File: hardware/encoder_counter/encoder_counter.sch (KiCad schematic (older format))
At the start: 29 parts, among them P1 MOLEX_HEADER, P10 FEMALE_HEADER, P11 TERM_BLOCK_CON, P2 MOLEX_HEADER, P3 FEMALE_HEADER, P4 FEMALE_HEADER, P5 MOLEX_HEADER, P6 MOLEX_HEADER, P7 FEMALE_HEADER, P8 FEMALE_HEADER, P9 CONN_01X03, U1 LM7812, U5 LS7366R, U6 LS7366R, Y1 20 MHz, Y2 20 MHz

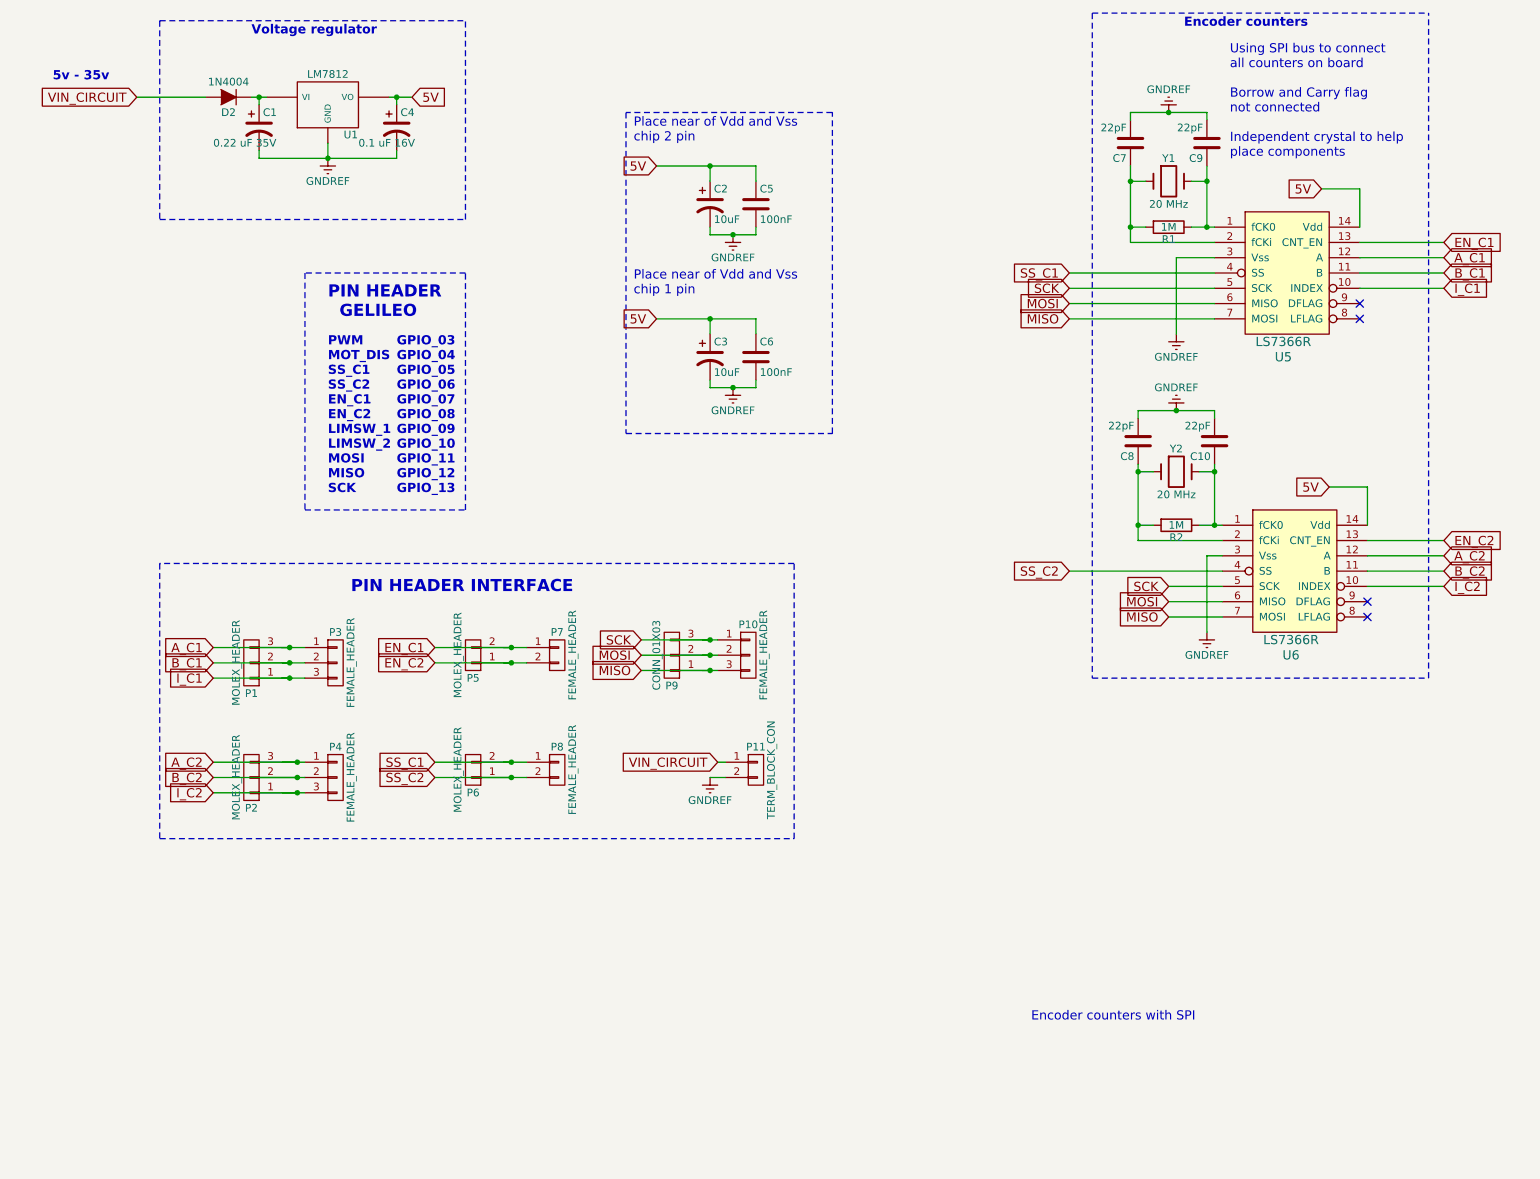
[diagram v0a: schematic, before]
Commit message: Added PID, LS7366R lib and layout off DC Motor Driver PCB and Arduino Shied PCB.
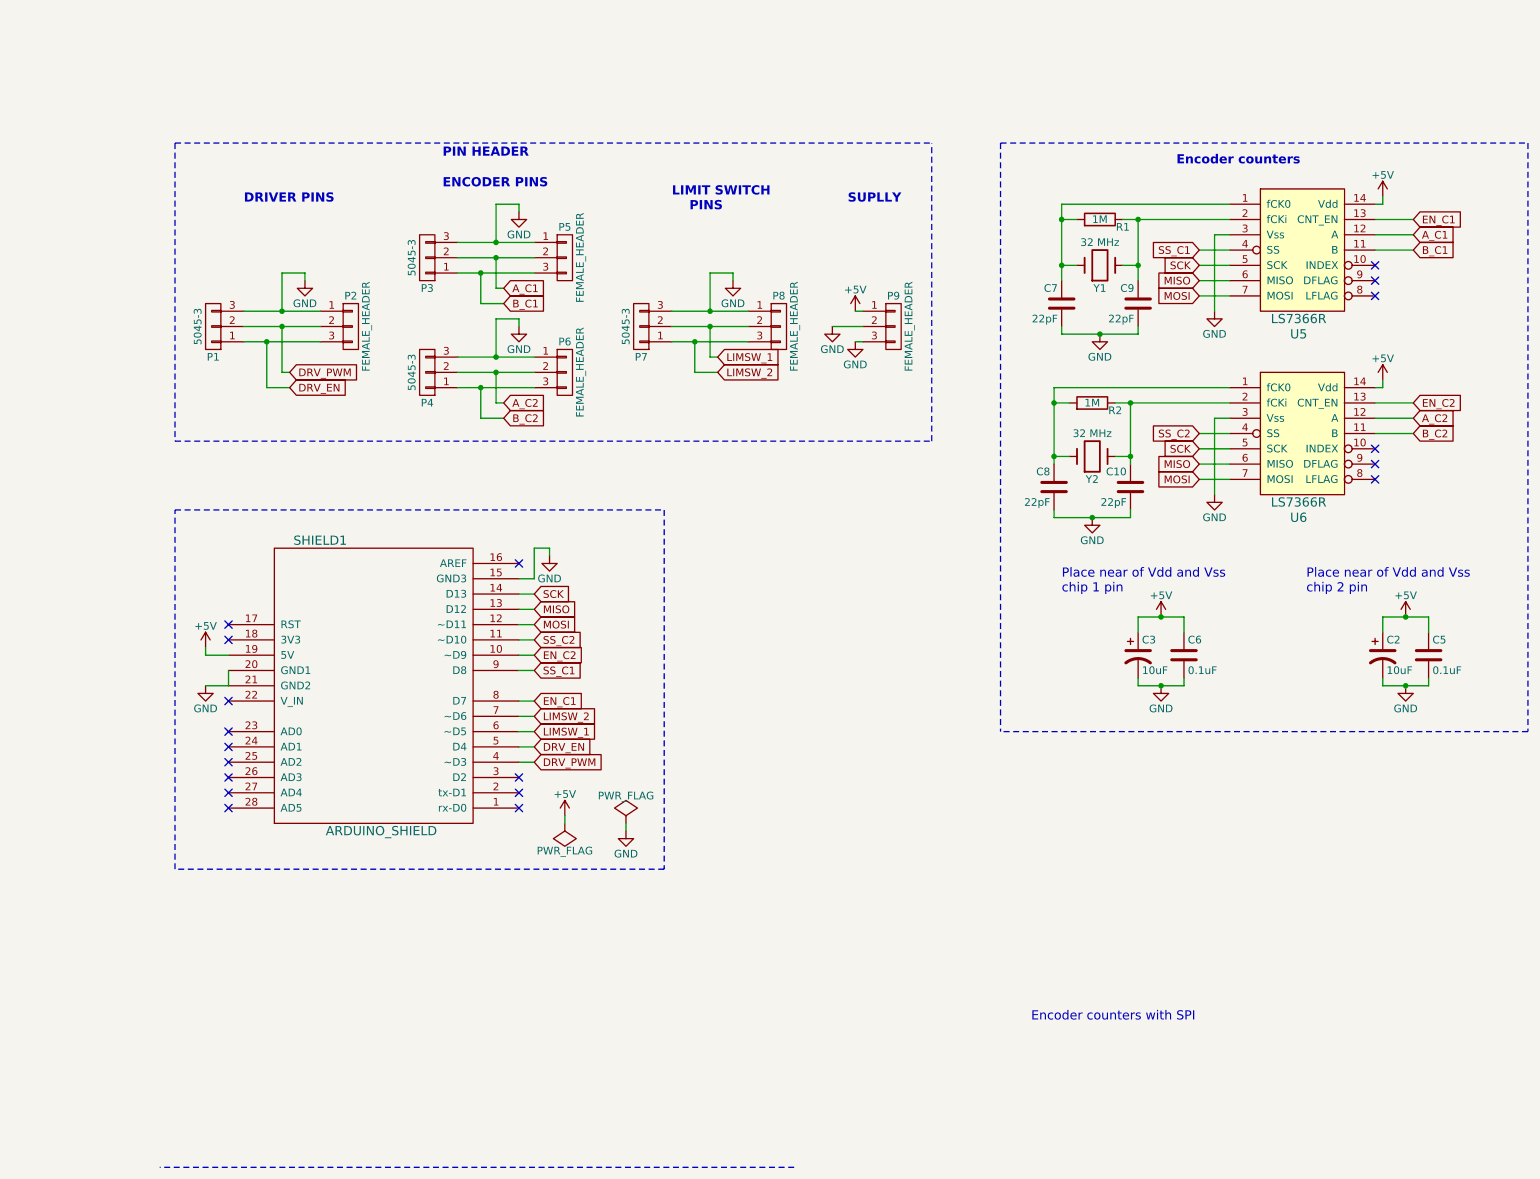
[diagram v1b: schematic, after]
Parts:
- removed C1: 0.22 uF 35V, symbol CP1
- removed C4: 0.1 uF 16V, symbol CP1
- removed D2: 1N4004, symbol D
- removed P10: FEMALE_HEADER, symbol CONN_01X03
- removed P11: TERM_BLOCK_CON, symbol CONN_01X02
- removed P5, P6: MOLEX_HEADER, symbol CONN_01X02
- removed P7, P8: FEMALE_HEADER, symbol CONN_01X02
- removed U1: LM7812, symbol LM7812
- added P5, P6, P8: FEMALE_HEADER, Maplex_Misc:Pin_Header_Straight_1x03_Pitch2.54mm, symbol CONN_01X03
- added P7: 5045-3, Maplex_Misc:Molex_3Pin_180_TH, symbol CONN_01X03
- added SHIELD1: ARDUINO_SHIELD, Maplex_Misc:ARDUINO_SHIELD, symbol ARDUINO_SHIELD
- C10, C7, C8, C9: footprint (none) -> Maplex_Misc:C_Disc_D3.4mm_W2.1mm_P2.50mm
- C2, C3: footprint (none) -> Maplex_Misc:CP_Radial_D6.3mm_P2.50mm
- C5, C6: value 100nF -> 0.1uF; footprint (none) -> Maplex_Misc:C_Disc_D5.0mm_W2.5mm_P2.50mm
- P1: value MOLEX_HEADER -> 5045-3; footprint (none) -> Maplex_Misc:Molex_3Pin_180_TH
- P2: value MOLEX_HEADER -> FEMALE_HEADER; footprint (none) -> Maplex_Misc:Pin_Header_Straight_1x03_Pitch2.54mm
- P3, P4: value FEMALE_HEADER -> 5045-3; footprint (none) -> Maplex_Misc:Molex_3Pin_180_TH
- P9: value CONN_01X03 -> FEMALE_HEADER; footprint (none) -> Maplex_Misc:Pin_Header_Straight_1x03_Pitch2.54mm
- R1, R2: footprint (none) -> Maplex_Misc:Resistor_Horizontal_RM10mm_L7mm
- U5, U6: footprint (none) -> Maplex_Misc:DIP-14_W15.24mm_Socket_Header
- Y1, Y2: value 20 MHz -> 32 MHz; footprint (none) -> Maplex_Misc:Crystal_HC18-U_Vertical
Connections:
- net A_C1: now also P3.2 (P2), P5.2 (P2); no longer P1.3 (P3), P3.1 (P1)
- net A_C2: now also P4.2 (P2), P6.2 (P2); no longer P2.3 (P3), P4.1 (P1)
- net B_C1: now also P3.1 (P1), P5.3 (P3); no longer P1.2 (P2), P3.2 (P2)
- net B_C2: now also P4.1 (P1), P6.3 (P3); no longer P2.2 (P2), P4.2 (P2)
- net EN_C1: now also SHIELD1.8 (D7)
- net EN_C2: now also SHIELD1.10 (~~D9)
- net MISO: now also U5.6 (MISO), U6.6 (MISO), SHIELD1.13 (D12); no longer P9.1 (P1), U5.7 (MOSI), U6.7 (MOSI)
- net MOSI: now also U5.7 (MOSI), U6.7 (MOSI), SHIELD1.12 (~~D11); no longer P9.2 (P2), U5.6 (MISO), U6.6 (MISO)
- net SCK: now also SHIELD1.14 (D13); no longer P9.3 (P3)
- net SS_C1: now also SHIELD1.9 (D8)
- net SS_C2: now also SHIELD1.11 (~~D10)
- net at C9.1, R1.1, Y1.2: now also U5.2 (fCKi); no longer U5.1 (fCK0)
- net at C7.1, R1.2, Y1.1: now also U5.1 (fCK0); no longer U5.2 (fCKi)
- net at C10.1, R2.1, Y2.2: now also U6.2 (fCKi); no longer U6.1 (fCK0)
- net at C8.1, R2.2, Y2.1: now also U6.1 (fCK0); no longer U6.2 (fCKi)
- net 5V renamed +5V
- net +5V: now also P9.1 (P1), SHIELD1.19 (5V)
- net GNDREF renamed GND
- net GND: now also P1.3 (P3), P2.1 (P1), P3.3 (P3), P4.3 (P3), P9.2 (P2), P9.3 (P3), P5.1 (P1), P6.1 (P1), P7.3 (P3), P8.1 (P1), SHIELD1.15 (GND3), SHIELD1.20 (GND1), SHIELD1.21 (GND2)
- removed net I_C1: P1.1 (P1), P3.3 (P3), U5.10 (INDEX)
- removed net I_C2: P2.1 (P1), P4.3 (P3), U6.10 (INDEX)
- new net DRV_EN: P1.1 (P1), P2.3 (P3), SHIELD1.5 (D4)
- new net DRV_PWM: P1.2 (P2), P2.2 (P2), SHIELD1.4 (~~D3)
- new net LIMSW_1: P7.2 (P2), P8.2 (P2), SHIELD1.6 (~~D5)
- new net LIMSW_2: P7.1 (P1), P8.3 (P3), SHIELD1.7 (~~D6)
- no-connect marks 4 -> 19
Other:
- note added: "DRIVER PINS"
- note added: "ENCODER PINS"
- note added: "LIMIT SWITCH\n PINS"
- note added: "PIN HEADER"
- note added: "SUPLLY"
- note removed: "5v - 35v"
- note removed: "GPIO_03\nGPIO_04\nGPIO_05\nGPIO_06\nGPIO_07\nGPIO_08\nGPIO_09\nGPIO_10\nGPIO_11\nGPIO_12\nGPIO_13"
- note removed: "PIN HEADER INTERFACE"
- note removed: "PIN HEADER\n GELILEO"
- note removed: "PWM\nMOT_DIS\nSS_C1\nSS_C2\nEN_C1\nEN_C2\nLIMSW_1\nLIMSW_2\nMOSI\nMISO\nSCK"
- note removed: "Using SPI bus to connect\nall counters on board\n\nBorrow and Carry flag\nnot connected\n\nIndependent crystal to help \nplace components"
- note removed: "Voltage regulator"
- moved on the sheet: C10, C2, C3, C5, C6, C7, C8, C9, R1, R2, U5, U6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

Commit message: Last version.
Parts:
- removed P1, P3, P4, P7: 5045-3, Maplex_Misc:Molex_3Pin_180_TH, symbol CONN_01X03
- removed P2, P5, P6, P8, P9: FEMALE_HEADER, Maplex_Misc:Pin_Header_Straight_1x03_Pitch2.54mm, symbol CONN_01X03
- SHIELD1: value ARDUINO_SHIELD -> GALILEO_SHIELD
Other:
- note removed: "DRIVER PINS"
- note removed: "ENCODER PINS"
- note removed: "LIMIT SWITCH\n PINS"
- note removed: "PIN HEADER"
- note removed: "SUPLLY"
- moved on the sheet: C10, C2, C3, C5, C6, C7, C8, C9, R1, R2, SHIELD1, U5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
